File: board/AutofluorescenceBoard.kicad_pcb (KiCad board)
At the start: 4 copper layers, 44.4 x 44.5 mm, 40 parts, among them J1 2002411212, Q1 BSS138, U1 PAM2863ECR, U2 PAM2863ECR, U3 PAM2863ECR

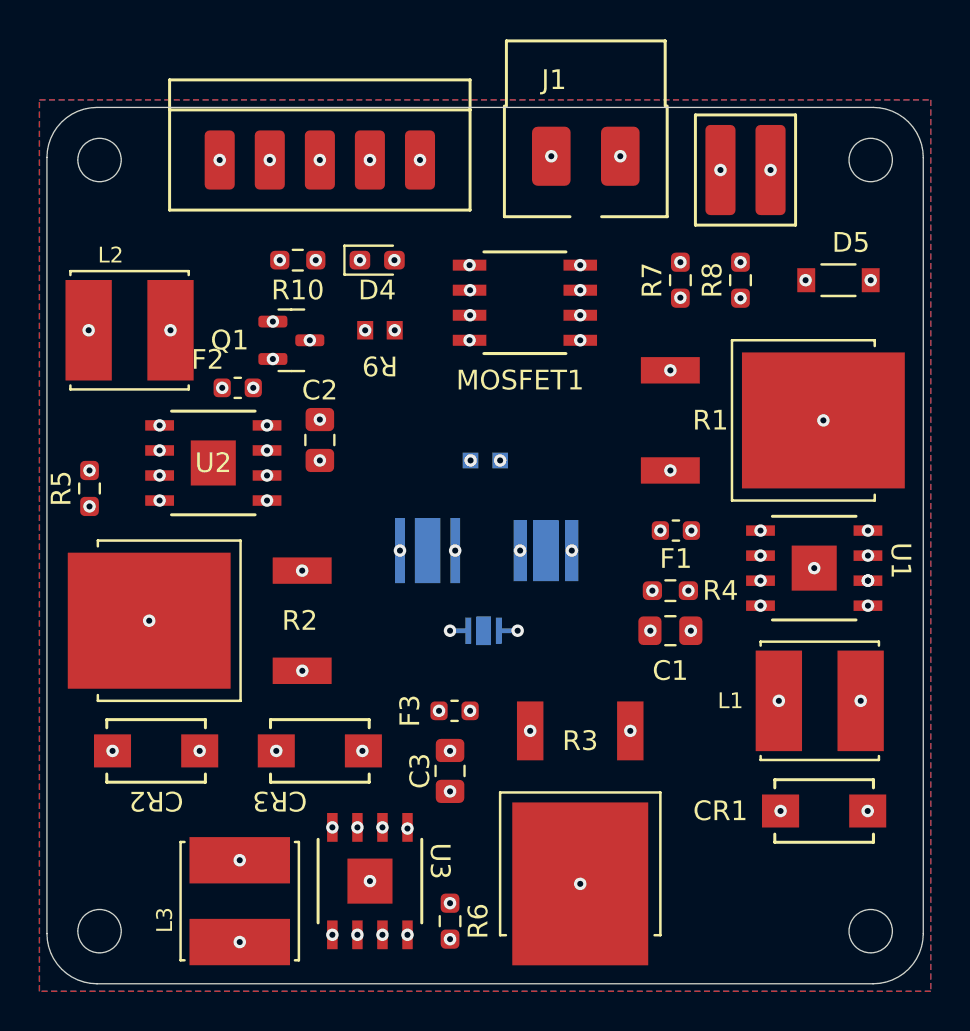
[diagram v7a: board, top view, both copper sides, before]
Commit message: Fixed Layout
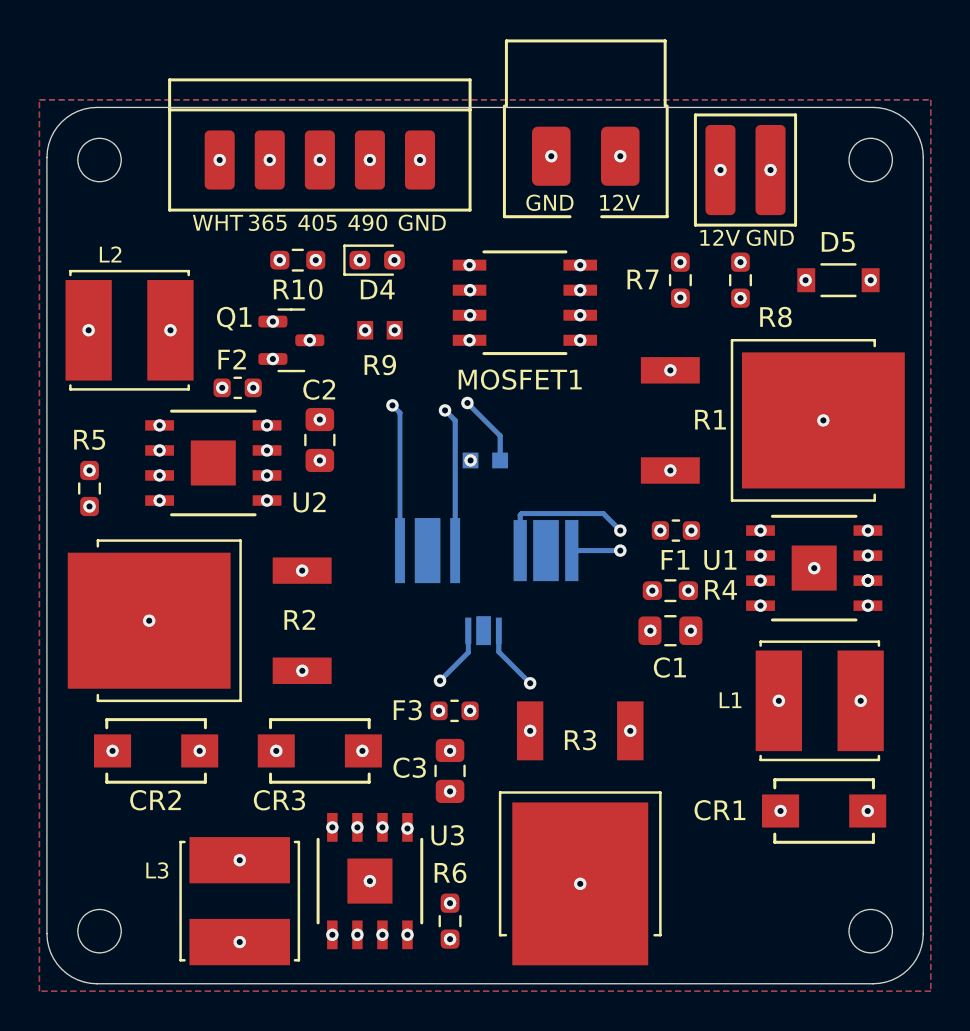
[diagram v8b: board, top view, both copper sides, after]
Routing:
- net ISET 405nm: track 50.7 -> 35.2 mm
- net Net-(U2-ISENSE): track 15.4 -> 22.1 mm
- net Net-(CR2-Pad2): track 47.0 -> 53.1 mm
- net Net-(D3-Pad1): track 28.8 -> 34.1 mm
- net Net-(D2-Pad1): track 23.8 -> 28.0 mm
- net Net-(D2-Pad2): track 12.0 -> 15.0 mm
- net Net-(MOSFET1-GATE): track 24.7 -> 27.0 mm
- net Net-(D1-Pad2): track 7.53 -> 9.30 mm
- net Net-(D1-Pad1): track 15.0 -> 16.4 mm
- net ISET 365nm: track 36.3 -> 37.1 mm
- net Net-(D3-Pad2): track 5.22 -> 4.68 mm
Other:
- board text added: "12V"
- board text added: "365"
- board text added: "405"
- board text added: "490"
- board text added: "GND"
- board text added: "WHT"
